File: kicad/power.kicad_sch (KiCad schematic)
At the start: 16 parts, among them J5 Conn_Coaxial_Power, J6 Screw_Terminal_01x02, U7 LD39150DT33, U8 TPS22917DBV, U9 TLV70012_SOT23-5

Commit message: updates
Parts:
- added C26, C28: 4.7u, symbol Device:C
- added C27: 1u, symbol Device:C
- added R21: 1K, symbol Device:R_US
- added U11: TLV70025_SOT23-5, Package_TO_SOT_SMD:SOT-23-5, symbol Regulator_Linear:TLV70025_SOT23-5
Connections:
- net +1V2: now also R21.1; no longer R22.1
- net GND: now also C26.2, C27.2, C28.2, U11.2 (GND)
- new net: C26.1, U11.1 (IN)
- new net +2V5: C28.1, R22.1, U11.5 (OUT)
- new net 2V5EN: C27.1, R21.2, U11.3 (EN)
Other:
- moved on the sheet: C16, C17, C18, C19, C20, C21, C7, C8, F1, J5, J6, R19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

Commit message: updates
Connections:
- net 3.3V_EARLY: now also C26.1, U11.1 (IN)
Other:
- moved on the sheet: C16, C17, C18, C19, C20, C21, C26, C27, C28, R19, R21, R22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

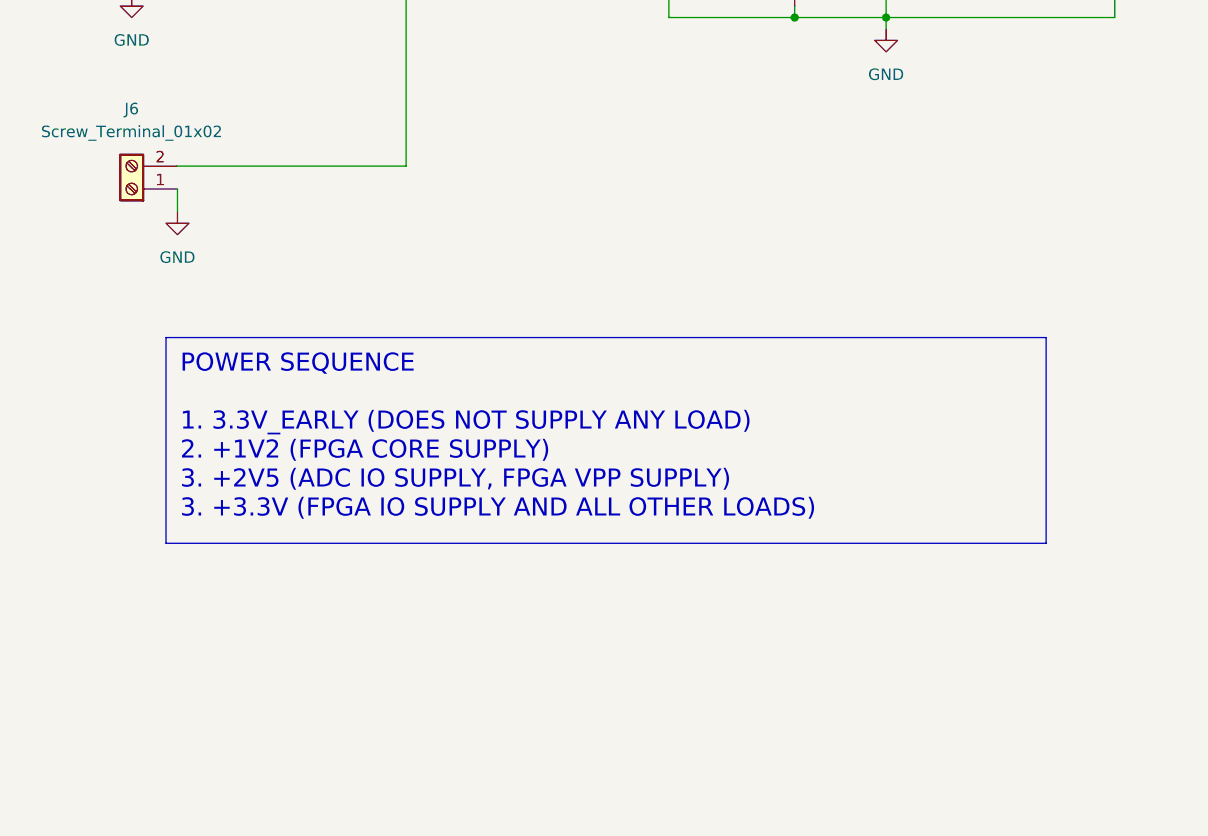
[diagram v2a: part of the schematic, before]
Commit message: wire up mcu
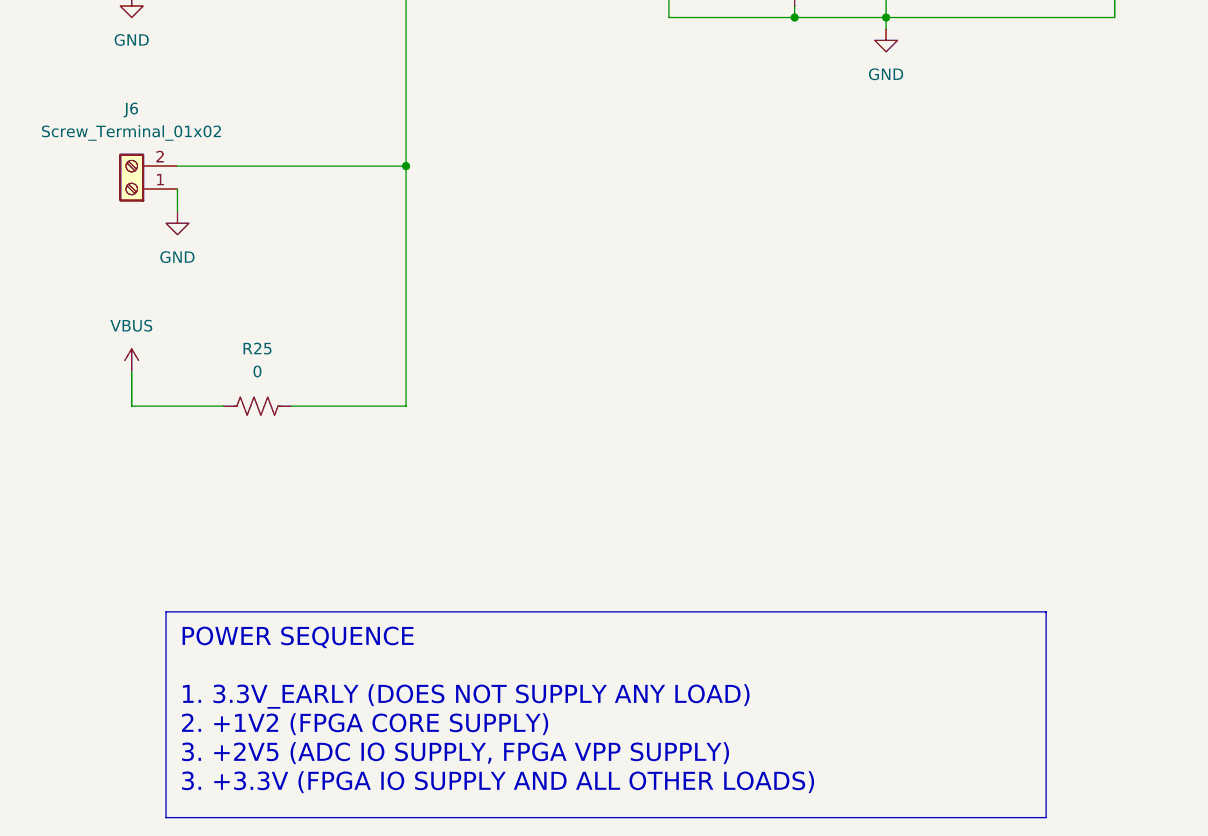
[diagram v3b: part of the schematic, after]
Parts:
- added R25: 0, symbol Device:R_US
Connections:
- net VIN: now also R25.1
- new net VBUS: R25.2
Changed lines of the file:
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@@
   (junction (at 255.27 72.39) (diameter 0) (color 0 0 0 0)
   )
+  (junction (at 66.04 72.39) (diameter 0) (color 0 0 0 0)
+  )
   (junction (at 182.88 41.91) (diameter 0) (color 0 0 0 0)
   )
@@
     (stroke (width 0) (type default))
   )
+  (wire (pts (xy 66.04 99.06) (xy 66.04 72.39))
+    (stroke (width 0) (type default))
+  )
   (wire (pts (xy 119.38 49.53) (xy 119.38 55.88))
     (stroke (width 0) (type default))
@@
     (stroke (width 0) (type default))
   )
+  (wire (pts (xy 35.56 95.25) (xy 35.56 99.06))
+    (stroke (width 0) (type default))
+  )
+  (wire (pts (xy 35.56 99.06) (xy 45.72 99.06))
+    (stroke (width 0) (type default))
+  )
   (wire (pts (xy 172.72 113.03) (xy 172.72 72.39))
     (stroke (width 0) (type default))
@@
     (stroke (width 0) (type default))
   )
+  (wire (pts (xy 53.34 99.06) (xy 66.04 99.06))
+    (stroke (width 0) (type default))
+  )
   (wire (pts (xy 109.22 55.88) (xy 119.38 55.88))
     (stroke (width 0) (type default))
@@
   )
   (text_box "POWER SEQUENCE\n\n1. 3.3V_EARLY (DOES NOT SUPPLY ANY LOAD)\n2. +1V2 (FPGA CORE SUPPLY)\n3. +2V5 (ADC IO SUPPLY, FPGA VPP SUPPLY)\n3. +3.3V (FPGA IO SUPPLY AND ALL OTHER LOADS)\n"
-    (at 39.37 91.44 0) (size 97.79 22.86)
+    (at 39.37 121.92 0) (size 97.79 22.86)
     (stroke (width 0) (type default))
     (fill (type none))
@@
     )
   )
+  (symbol (lib_id "power:VBUS") (at 35.56 95.25 0) (unit 1)
+    (in_bom yes) (on_board yes) (dnp no) (fields_autoplaced)
+    (property "Reference" "#PWR078" (at 35.56 99.06 0)
+      (effects (font (size 1.27 1.27)) hide)
+    )
+    (property "Value" "VBUS" (at 35.56 90.17 0)
+      (effects (font (size 1.27 1.27)))
+    )
+    (property "Footprint" "" (at 35.56 95.25 0)
+      (effects (font (size 1.27 1.27)) hide)
+    )
+    (property "Datasheet" "" (at 35.56 95.25 0)
+      (effects (font (size 1.27 1.27)) hide)
+    )
+    (pin "1")
+    (instances
+      (project "gpsrx"
+        (path "/c3c549bc-9d82-4b6a-bdb9-a3870905229d/1b4527d9-1a53-4872-9983-970267f23268"
+          (reference "#PWR078") (unit 1)
+        )
+      )
+    )
+  )
   (symbol (lib_id "Regulator_Linear:LD39150DT33") (at 119.38 41.91 0) (unit 1)
     (in_bom yes) (on_board yes) (dnp no) (fields_autoplaced)
@@
         )
       )
+    )
+  )
+  (symbol (lib_id "Device:R_US") (at 49.53 99.06 270) (unit 1)
+    (in_bom yes) (on_board no) (dnp no) (fields_autoplaced)
+    (property "Reference" "R25" (at 49.53 92.71 90)
+      (effects (font (size 1.27 1.27)))
+    )
+    (property "Value" "0" (at 49.53 95.25 90)
+      (effects (font (size 1.27 1.27)))
+    )
+    (property "Footprint" "" (at 49.276 100.076 90)
+      (effects (font (size 1.27 1.27)) hide)
+    )
+    (property "Datasheet" "~" (at 49.53 99.06 0)
+      (effects (font (size 1.27 1.27)) hide)
+    )
+    (pin "2")
+    (pin "1")
+    (instances
+      (project "gpsrx"
+        (path "/c3c549bc-9d82-4b6a-bdb9-a3870905229d/1b4527d9-1a53-4872-9983-970267f23268"
+          (reference "R25") (unit 1)
+        )
+      )

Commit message: fix ercs
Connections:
- no-connect marks 0 -> 1
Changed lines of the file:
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@@
   (junction (at 194.31 113.03) (diameter 0) (color 0 0 0 0)
   )
+  (junction (at 41.91 99.06) (diameter 0) (color 0 0 0 0)
+  )
   (junction (at 95.25 41.91) (diameter 0) (color 0 0 0 0)
   )
   (junction (at 182.88 72.39) (diameter 0) (color 0 0 0 0)
   )
-  (junction (at 247.65 72.39) (diameter 0) (color 0 0 0 0)
-  )
   (junction (at 251.46 113.03) (diameter 0) (color 0 0 0 0)
   )
@@
   (junction (at 172.72 72.39) (diameter 0) (color 0 0 0 0)
   )
-  (junction (at 134.62 41.91) (diameter 0) (color 0 0 0 0)
-  )
   (junction (at 172.72 41.91) (diameter 0) (color 0 0 0 0)
   )
@@
   (junction (at 144.78 41.91) (diameter 0) (color 0 0 0 0)
   )
-  (junction (at 247.65 41.91) (diameter 0) (color 0 0 0 0)
-  )
   (junction (at 255.27 72.39) (diameter 0) (color 0 0 0 0)
   )
@@
   (junction (at 236.22 72.39) (diameter 0) (color 0 0 0 0)
   )
-  (junction (at 109.22 55.88) (diameter 0) (color 0 0 0 0)
-  )
-  (junction (at 247.65 113.03) (diameter 0) (color 0 0 0 0)
-  )
+  (no_connect (at 238.76 115.57))
   (wire (pts (xy 233.68 41.91) (xy 236.22 41.91))
     (stroke (width 0) (type default))
   )
-  (wire (pts (xy 236.22 72.39) (xy 247.65 72.39))
+  (wire (pts (xy 236.22 72.39) (xy 255.27 72.39))
     (stroke (width 0) (type default))
   )
@@
     (stroke (width 0) (type default))
   )
-  (wire (pts (xy 247.65 41.91) (xy 255.27 41.91))
+  (wire (pts (xy 236.22 41.91) (xy 255.27 41.91))
     (stroke (width 0) (type default))
   )
@@
     (stroke (width 0) (type default))
   )
-  (wire (pts (xy 236.22 41.91) (xy 247.65 41.91))
-    (stroke (width 0) (type default))
-  )
   (wire (pts (xy 204.47 115.57) (xy 194.31 115.57))
     (stroke (width 0) (type default))
@@
     (stroke (width 0) (type default))
   )
-  (wire (pts (xy 247.65 113.03) (xy 251.46 113.03))
-    (stroke (width 0) (type default))
-  )
   (wire (pts (xy 204.47 44.45) (xy 218.44 44.45))
     (stroke (width 0) (type default))
@@
     (stroke (width 0) (type default))
   )
-  (wire (pts (xy 247.65 72.39) (xy 255.27 72.39))
-    (stroke (width 0) (type default))
-  )
   (wire (pts (xy 195.58 44.45) (xy 189.23 44.45))
     (stroke (width 0) (type default))
@@
     (stroke (width 0) (type default))
   )
-  (wire (pts (xy 109.22 55.88) (xy 109.22 54.61))
+  (wire (pts (xy 41.91 99.06) (xy 45.72 99.06))
     (stroke (width 0) (type default))
   )
@@
     (stroke (width 0) (type default))
   )
-  (wire (pts (xy 35.56 99.06) (xy 45.72 99.06))
+  (wire (pts (xy 35.56 99.06) (xy 41.91 99.06))
     (stroke (width 0) (type default))
   )
@@
     (stroke (width 0) (type default))
   )
-  (wire (pts (xy 134.62 41.91) (xy 144.78 41.91))
+  (wire (pts (xy 127 41.91) (xy 144.78 41.91))
     (stroke (width 0) (type default))
   )
@@
     (stroke (width 0) (type default))
   )
-  (wire (pts (xy 127 41.91) (xy 134.62 41.91))
-    (stroke (width 0) (type default))
-  )
   (wire (pts (xy 35.56 52.07) (xy 35.56 53.34))
     (stroke (width 0) (type default))
@@
     (stroke (width 0) (type default))
   )
-  (wire (pts (xy 109.22 55.88) (xy 119.38 55.88))
+  (wire (pts (xy 95.25 55.88) (xy 119.38 55.88))
     (stroke (width 0) (type default))
   )
@@
     (stroke (width 0) (type default))
   )
-  (wire (pts (xy 95.25 55.88) (xy 109.22 55.88))
-    (stroke (width 0) (type default))
-  )
   (wire (pts (xy 265.43 111.76) (xy 265.43 113.03))
     (stroke (width 0) (type default))
@@
     (stroke (width 0) (type default))
   )
-  (wire (pts (xy 238.76 113.03) (xy 247.65 113.03))
+  (wire (pts (xy 238.76 113.03) (xy 251.46 113.03))
     (stroke (width 0) (type default))
   )
@@
     )
   )
-  (symbol (lib_id "power:PWR_FLAG") (at 109.22 54.61 0) (unit 1)
-    (in_bom yes) (on_board yes) (dnp no) (fields_autoplaced)
-    (property "Reference" "#FLG02" (at 109.22 52.705 0)
-      (effects (font (size 1.27 1.27)) hide)
-    )
-    (property "Value" "PWR_FLAG" (at 109.22 49.53 0)
-      (effects (font (size 1.27 1.27)))
-    )
-    (property "Footprint" "" (at 109.22 54.61 0)
-      (effects (font (size 1.27 1.27)) hide)
-    )
-    (property "Datasheet" "~" (at 109.22 54.61 0)
-      (effects (font (size 1.27 1.27)) hide)
-    )
-    (pin "1")
-    (instances
-      (project "gpsrx"
-        (path "/c3c549bc-9d82-4b6a-bdb9-a3870905229d/1b4527d9-1a53-4872-9983-970267f23268"
-          (reference "#FLG02") (unit 1)
-        )
-      )
-    )
-  )
   (symbol (lib_id "power:GND") (at 182.88 50.8 0) (unit 1)
     (in_bom yes) (on_board yes) (dnp no) (fields_autoplaced)
@@
     )
   )
-  (symbol (lib_id "power:PWR_FLAG") (at 247.65 72.39 0) (unit 1)
-    (in_bom yes) (on_board yes) (dnp no) (fields_autoplaced)
-    (property "Reference" "#FLG07" (at 247.65 70.485 0)
-      (effects (font (size 1.27 1.27)) hide)
-    )
-    (property "Value" "PWR_FLAG" (at 247.65 67.31 0)
-      (effects (font (size 1.27 1.27)))
-    )
-    (property "Footprint" "" (at 247.65 72.39 0)
-      (effects (font (size 1.27 1.27)) hide)
-    )
-    (property "Datasheet" "~" (at 247.65 72.39 0)
-      (effects (font (size 1.27 1.27)) hide)
-    )
-    (pin "1")
-    (instances
-      (project "gpsrx"
-        (path "/c3c549bc-9d82-4b6a-bdb9-a3870905229d/1b4527d9-1a53-4872-9983-970267f23268"
-          (reference "#FLG07") (unit 1)
-        )
-      )
-    )
-  )
   (symbol (lib_id "Regulator_Linear:TLV70012_SOT23-5") (at 226.06 44.45 0) (unit 1)
     (in_bom yes) (on_board yes) (dnp no)
@@
     )
   )
-  (symbol (lib_id "power:PWR_FLAG") (at 247.65 113.03 0) (unit 1)
-    (in_bom yes) (on_board yes) (dnp no) (fields_autoplaced)
-    (property "Reference" "#FLG05" (at 247.65 111.125 0)
-      (effects (font (size 1.27 1.27)) hide)
-    )
-    (property "Value" "PWR_FLAG" (at 247.65 107.95 0)
-      (effects (font (size 1.27 1.27)))
-    )
-    (property "Footprint" "" (at 247.65 113.03 0)
-      (effects (font (size 1.27 1.27)) hide)
-    )
-    (property "Datasheet" "~" (at 247.65 113.03 0)
-      (effects (font (size 1.27 1.27)) hide)
-    )
-    (pin "1")
-    (instances
-      (project "gpsrx"
-        (path "/c3c549bc-9d82-4b6a-bdb9-a3870905229d/1b4527d9-1a53-4872-9983-970267f23268"
-          (reference "#FLG05") (unit 1)
-        )
-      )
-    )
-  )
   (symbol (lib_id "power:GND") (at 204.47 52.07 0) (unit 1)
     (in_bom yes) (on_board yes) (dnp no) (fields_autoplaced)
@@
         (path "/c3c549bc-9d82-4b6a-bdb9-a3870905229d/1b4527d9-1a53-4872-9983-970267f23268"
           (reference "#PWR044") (unit 1)
+        )
+      )
+    )
+  )
+  (symbol (lib_id "power:PWR_FLAG") (at 41.91 99.06 0) (unit 1)
+    (in_bom yes) (on_board yes) (dnp no) (fields_autoplaced)
+    (property "Reference" "#FLG01" (at 41.91 97.155 0)
+      (effects (font (size 1.27 1.27)) hide)
+    )
+    (property "Value" "PWR_FLAG" (at 41.91 93.98 0)
+      (effects (font (size 1.27 1.27)))
+    )
+    (property "Footprint" "" (at 41.91 99.06 0)
+      (effects (font (size 1.27 1.27)) hide)
+    )
+    (property "Datasheet" "~" (at 41.91 99.06 0)
+      (effects (font (size 1.27 1.27)) hide)
+    )
+    (pin "1")
+    (instances
+      (project "gpsrx"
+        (path "/c3c549bc-9d82-4b6a-bdb9-a3870905229d/1b4527d9-1a53-4872-9983-970267f23268"
+          (reference "#FLG01") (unit 1)
         )
       )
@@
     )
   )
-  (symbol (lib_id "power:PWR_FLAG") (at 134.62 41.91 0) (unit 1)
-    (in_bom yes) (on_board yes) (dnp no) (fields_autoplaced)
-    (property "Reference" "#FLG01" (at 134.62 40.005 0)
-      (effects (font (size 1.27 1.27)) hide)
-    )
-    (property "Value" "PWR_FLAG" (at 134.62 36.83 0)
-      (effects (font (size 1.27 1.27)))
-    )
-    (property "Footprint" "" (at 134.62 41.91 0)
-      (effects (font (size 1.27 1.27)) hide)
-    )
-    (property "Datasheet" "~" (at 134.62 41.91 0)
-      (effects (font (size 1.27 1.27)) hide)
-    )
-    (pin "1")
-    (instances
-      (project "gpsrx"
-        (path "/c3c549bc-9d82-4b6a-bdb9-a3870905229d/1b4527d9-1a53-4872-9983-970267f23268"
-          (reference "#FLG01") (unit 1)
-        )
-      )
-    )
-  )
   (symbol (lib_id "power:+1V2") (at 267.97 41.91 0) (unit 1)
     (in_bom yes) (on_board yes) (dnp no) (fields_autoplaced)
@@
         )
       )
-    )
-  )
-  (symbol (lib_id "power:PWR_FLAG") (at 247.65 41.91 0) (unit 1)
-    (in_bom yes) (on_board yes) (dnp no) (fields_autoplaced)
-    (property "Reference" "#FLG06" (at 247.65 40.005 0)
-      (effects (font (size 1.27 1.27)) hide)
-    )
-    (property "Value" "PWR_FLAG" (at 247.65 36.83 0)
-      (effects (font (size 1.27 1.27)))
-    )
-    (property "Footprint" "" (at 247.65 41.91 0)
-      (effects (font (size 1.27 1.27)) hide)
-    )
-    (property "Datasheet" "~" (at 247.65 41.91 0)
-      (effects (font (size 1.27 1.27)) hide)
-    )
-    (pin "1")
-    (instances
-      (project "gpsrx"
-        (path "/c3c549bc-9d82-4b6a-bdb9-a3870905229d/1b4527d9-1a53-4872-9983-970267f23268"
-          (reference "#FLG06") (unit 1)
-        )
-      )

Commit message: power and frontend updates
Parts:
- removed U11: TLV70025_SOT23-5, Package_TO_SOT_SMD:SOT-23-5, symbol Regulator_Linear:TLV70025_SOT23-5
- removed U7: LD39150DT33, Package_TO_SOT_SMD:TO-252-3_TabPin2, symbol Regulator_Linear:LD39150DT33
- removed U8: TPS22917DBV, Package_TO_SOT_SMD:SOT-23-6, symbol Power_Management:TPS22917DBV
- removed U9: TLV70012_SOT23-5, Package_TO_SOT_SMD:SOT-23-5, symbol Regulator_Linear:TLV70012_SOT23-5
- added C65, C66, C67, C71: 1u, symbol Device:C
- added C68, C70: 2.2u, symbol Device:C
- added C69: 100u, symbol Device:C
- added R65, R74: 1K, symbol Device:R_US
- added R66, R67: 0, symbol Device:R_US
- added R68: 2.55K, symbol Device:R_US
- added R69: 10.2K, symbol Device:R_US
- added R70: 6.34K, symbol Device:R_US
- added R71: 2.0K, symbol Device:R_US
- added R72: 17.8K, symbol Device:R_US
- added R73: 10K, symbol Device:R_US
- added R75: 9.09K, symbol Device:R_US
- added R76: 47.5K, symbol Device:R_US
- added R77: 78.7K, symbol Device:R_US
- added U11, U22, U8, U9: ADP7118ACPZN, Package_CSP:LFCSP-6-1EP_2x2mm_P0.65mm_EP1x1.6mm, symbol Regulator_Linear:ADP7118ACPZN
- added U24: MIC2025-2YM, Package_SO:SOIC-8_3.9x4.9mm_P1.27mm, symbol Power_Management:MIC2025-2YM
- added U7: LTM8078EY-PBF, LTM8078IY-PBF_ADI, symbol bgelb_lib:LTM8078EY-PBF
- C16, C17, C26, C8: value 4.7u -> 1u
- C18, C28: value 4.7u -> 2.2u
- C19: value 100p -> 1u; now fitted
- C7: value 4.7u -> 100u
- R21: value 1K -> 2K
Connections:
- net +1V2: now also R66.1, U9.1 (VOUT); no longer R21.1
- net +2V5: now also R68.1, R74.1, U11.1 (VOUT); no longer R22.1
- net +3.3V: now also C17.1, C26.1, C7.1, R19.1, R21.1, U11.6 (VIN), U24.7 (IN), U7.F1 (VOUT1), U7.F2 (VOUT1), U7.G1 (VOUT1), U7.G2 (VOUT1), U9.6 (VIN)
- net 1V2EN: now also U9.4 (EN)
- net 2V5EN: now also U11.4 (EN)
- net GND: now also C19.2, C65.2, C66.2, C67.2, C68.2, C69.2, C70.2, C71.2, R67.2, R69.2, R71.2, R73.2, R75.2, R76.2, R77.2, U11.3 (GND), U11.7 (GND), U22.3 (GND), U22.7 (GND), U24.3 (GND), U7.A1 (GND), U7.A7 (GND), U7.B2 (GND), U7.B3 (GND), U7.B4 (GND), U7.B5 (GND), U7.C2 (GND), U7.C3 (GND), U7.C4 (GND), U7.C5 (GND), U7.D2 (GND), U7.D3 (GND), U7.D4 (GND), U7.D5 (GND), U7.E1 (GND), U7.E2 (GND), U7.E3 (GND), U7.E4 (GND), U7.E5 (GND), U7.E6 (GND), U7.F3 (GND), U7.F4 (GND), U7.F5 (GND), U7.G3 (GND), U7.G4 (GND), U7.G5 (GND), U8.3 (GND), U8.7 (GND), U9.3 (GND), U9.7 (GND)
- net VIN_FUSED: now also C65.1, U7.A3 (VIN1), U7.A4 (VIN2), U7.A5 (RUN)
- net 3V3A_EN: now reaches C20.1, R22.2
- net 3V3A_EN: now also U8.4 (EN)
- removed net 3.3V_EARLY: C17.1, C19.1, C26.1, C7.1, R19.1
- new net: R66.2, R67.1, U9.2 (SENSE/ADJ)
- new net: R72.2, R73.1, U8.2 (SENSE/ADJ)
- new net: R68.2, R69.1, U11.2 (SENSE/ADJ)
- new net: R70.2, R71.1, U22.2 (SENSE/ADJ)
- new net: R76.1, U7.C7 (FB2)
- new net: R75.1, U7.B7 (RT)
- new net: U7.C6 (OM), U7.D6 (OMC)
- new net: R77.1, U7.D7 (FB1)
- new net +3.3VA: C70.1, R72.1, U8.1 (VOUT)
- new net +3.3VP: U24.6 (OUT), U24.8 (OUT)
- new net +5VA: C68.1, R70.1, U22.1 (VOUT)
- new net 3V3IO_EN: C71.1, R74.2, U24.1 (EN)
- new net 5V5_OUT: C19.1, C66.1, C69.1, R22.1, R65.1, U22.6 (VIN), U7.E7 (BIAS), U7.F6 (VOUT2), U7.F7 (VOUT2), U7.G6 (VOUT2), U7.G7 (VOUT2), U8.6 (VIN)
- new net 5VA_EN: C67.1, R65.2, U22.4 (EN)
- no-connect marks 1 -> 11
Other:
- note added: "RC = 2ms"
- moved on the sheet: C17, C18, C21, C26, C27, C28, C7, C8, F1, J5, J6, R19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

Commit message: Tweaks
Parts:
- R76: value 47.5K -> 43.2K
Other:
- note added: "F_SW = 2.6MHz"
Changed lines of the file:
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@@
     (effects (font (size 2 2)) (justify left top))
+  )
+  (text "F_SW = 2.6MHz" (at 60.96 81.28 0)
+    (effects (font (size 1.27 1.27)) (justify left bottom))
   )
   (text "RC = 2ms" (at 210.82 68.58 0)
@@
       (effects (font (size 1.27 1.27)) (justify left))
     )
-    (property "Value" "47.5K" (at 81.28 99.06 0)
-      (effects (font (size 1.27 1.27)) (justify left))
-    )
+    (property "Value" "43.2K" (at 81.28 99.06 0)
+      (effects (font (size 1.27 1.27)) (justify left))
+    )
